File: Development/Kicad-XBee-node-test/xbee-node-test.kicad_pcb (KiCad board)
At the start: 2 copper layers, 90 x 50 mm, 48 parts, among them IC1 ATMEGA48-P, P1 Program, P2 Power 3.7V-12V, P3 Analogue, P4 Count, Q1 2N7002, Q2 BSS84, SW2 Commissioning, U1 TPS77033

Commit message: Minor tweaks on the PCBs ready to manufacture
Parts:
- added GND: GND, photodiode:SIL-1, F.Cu at (85.3, 96.7)
- added VRef: VRef, photodiode:SIL-1, F.Cu at (88.5, 68.4)
- moved G*** 1.31 mm to (71.7, 53.8)
- moved D1 0.77 mm to (82.5, 76.6)
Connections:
- D2 pad 1: GND -> Net-(D2-Pad1)
- D4 pad 1: GND -> Net-(D4-Pad1)
- D6 pad 1: GND -> Net-(D6-Pad1)
- D7 pad 1: GND -> Net-(D7-Pad1)
- R3 pad 1: Net-(D2-Pad2) -> Net-(R3-Pad1)
- R4 pad 1: Net-(D4-Pad2) -> Net-(R4-Pad1)
- R5 pad 1: Net-(D6-Pad2) -> Net-(R5-Pad1)
- R6 pad 1: Net-(D7-Pad2) -> Net-(R6-Pad1)
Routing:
- net Net-(D3-Pad1): track 3.08 -> 6.96 mm
- net Net-(R6-Pad1): track 0.00 -> 3.70 mm
- net Net-(R5-Pad1): track 0.00 -> 3.70 mm
- net Net-(R4-Pad1): track 0.00 -> 3.70 mm
- net Net-(R3-Pad1): track 0.00 -> 3.70 mm
- net Net-(D7-Pad2): track 4.78 -> 1.08 mm
- net Net-(D6-Pad2): track 4.78 -> 1.08 mm
- net Net-(D4-Pad2): track 4.78 -> 1.08 mm
- net Net-(D2-Pad2): track 4.78 -> 1.08 mm
- net /VBAT: track 87.6 -> 89.5 mm
- net /ARef: track 49.8 -> 50.7 mm
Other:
- board text added: "ATMega48/88/168/328"
- board text added: "Analogue"
- board text added: "Associate"
- board text added: "Commissioning"
- board text added: "Count"
- board text added: "Debug"
- board text added: "K. Sarkies Version 1 02/02/2017"
- board text added: "Power"
- board text added: "Power 3.7V - 12V"
- board text added: "Program"
- board text added: "Reset"
- board text added: "Test"
- board text added: "VRef Adjust"
- board text added: "XBee Node Test Board"

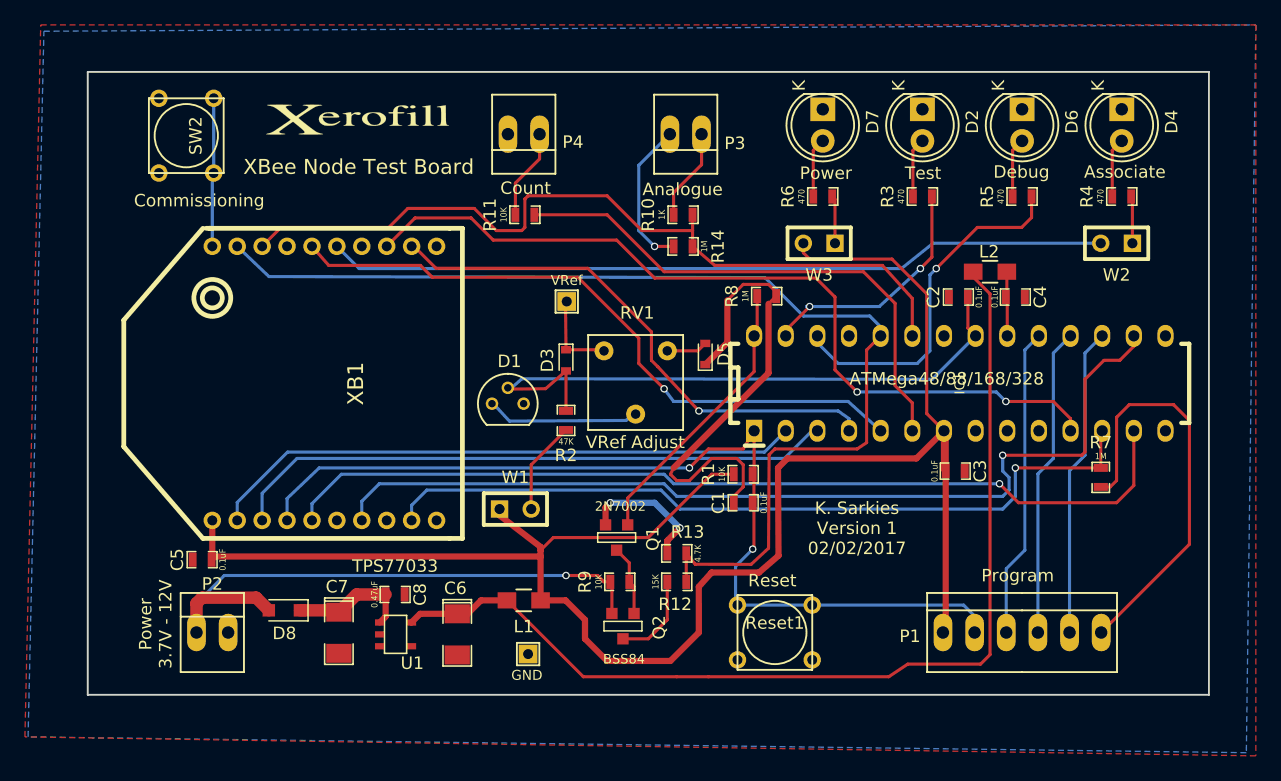
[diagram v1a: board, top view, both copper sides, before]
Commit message: Correct some stupid errors in Testboard and XBee-node-test PCBs.
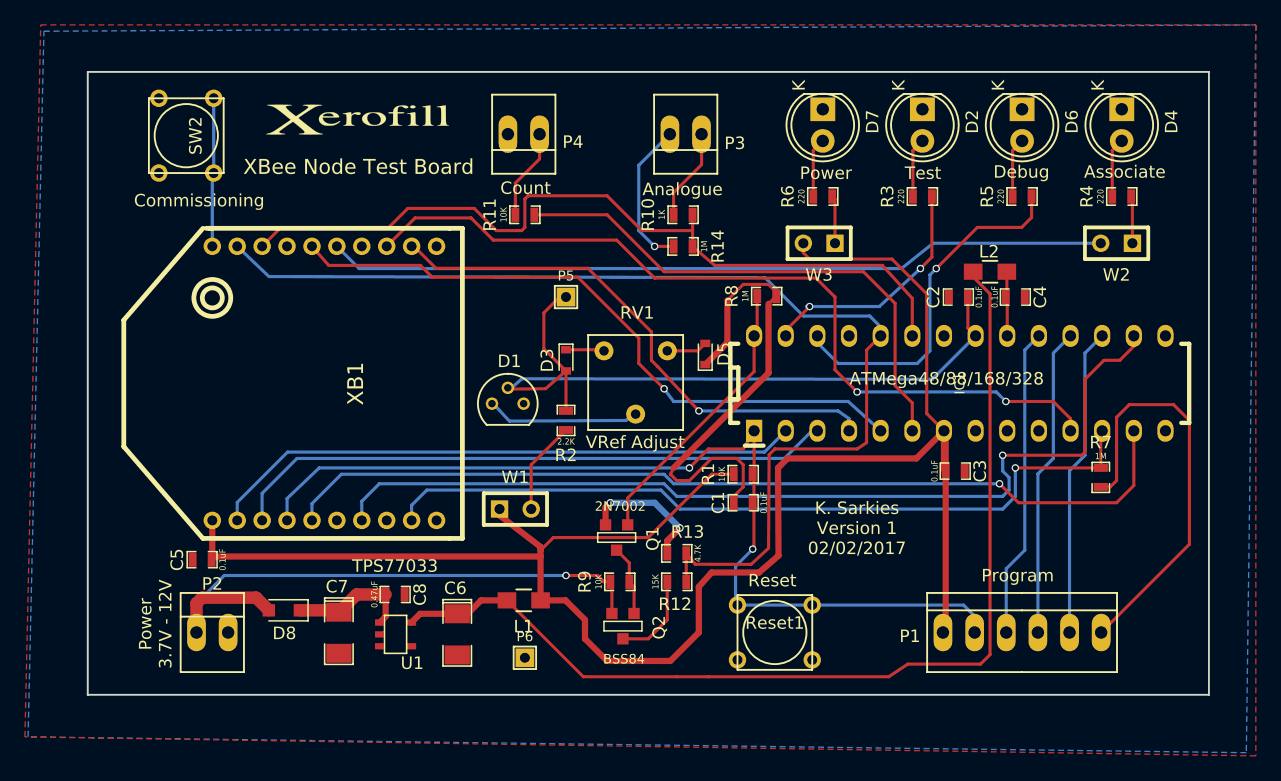
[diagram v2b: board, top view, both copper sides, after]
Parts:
- removed GND: GND, photodiode:SIL-1
- removed VRef: VRef, photodiode:SIL-1
- added P5: VRef, photodiode:SIL-1, F.Cu at (88.4, 68.1)
- added P6: GND, photodiode:SIL-1, F.Cu at (85.1, 97.0)
- D1: value LM336 -> LM336-2.5V
- D3, D5: value D -> 1N4148
- R2: value 47K -> 2.2K
- R3, R4, R5, R6: value 470 -> 220
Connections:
- D2 pad 1: Net-(D2-Pad1) -> GND
- D4 pad 1: Net-(D4-Pad1) -> GND
- D6 pad 1: Net-(D6-Pad1) -> GND
- D7 pad 1: Net-(D7-Pad1) -> GND
- R3 pad 1: Net-(R3-Pad1) -> Net-(D2-Pad2)
- R4 pad 1: Net-(R4-Pad1) -> Net-(D4-Pad2)
- R5 pad 1: Net-(R5-Pad1) -> Net-(D6-Pad2)
- R6 pad 1: Net-(R6-Pad1) -> Net-(D7-Pad2)
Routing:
- net /ARef: track 50.7 -> 58.4 mm
- net Net-(D3-Pad1): track 6.96 -> 3.08 mm
- net Net-(R6-Pad1): track 3.70 -> 0.00 mm
- net Net-(R5-Pad1): track 3.70 -> 0.00 mm
- net Net-(R4-Pad1): track 3.70 -> 0.00 mm
- net Net-(R3-Pad1): track 3.70 -> 0.00 mm
- net Net-(D7-Pad2): track 1.08 -> 4.78 mm
- net Net-(D6-Pad2): track 1.08 -> 4.78 mm
- net Net-(D4-Pad2): track 1.08 -> 4.78 mm
- net Net-(D2-Pad2): track 1.08 -> 4.78 mm
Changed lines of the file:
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@@
-(kicad_pcb (version 4) (host pcbnew 4.0.5-e0-6337~49~ubuntu16.04.1)
+(kicad_pcb (version 4) (host pcbnew 4.0.5-e0-6337~49~ubuntu14.04.1)
   (general
-    (links 95)
+    (links 103)
     (no_connects 0)
     (area 44.958 46.228 143.764001 104.902001)
     (thickness 1.6)
     (drawings 18)
-    (tracks 349)
+    (tracks 352)
     (zones 0)
     (modules 50)
-    (nets 61)
+    (nets 53)
   )
   (page A4)
   (layers
-    (0 F.Cu signal hide)
-    (31 B.Cu signal hide)
+    (0 F.Cu signal)
+    (31 B.Cu signal)
     (32 B.Adhes user hide)
     (33 F.Adhes user hide)
@@
   (net 51 "Net-(R4-Pad2)")
   (net 52 "Net-(R6-Pad2)")
-  (net 53 "Net-(D2-Pad1)")
-  (net 54 "Net-(D4-Pad1)")
-  (net 55 "Net-(D6-Pad1)")
-  (net 56 "Net-(D7-Pad1)")
-  (net 57 "Net-(R3-Pad1)")
-  (net 58 "Net-(R4-Pad1)")
-  (net 59 "Net-(R5-Pad1)")
-  (net 60 "Net-(R6-Pad1)")
   (net_class Default "This is the default net class."
     (clearance 0.2)
@@
     (add_net "Net-(C7-Pad1)")
     (add_net "Net-(D1-Pad1)")
-    (add_net "Net-(D2-Pad1)")
     (add_net "Net-(D2-Pad2)")
     (add_net "Net-(D3-Pad1)")
-    (add_net "Net-(D4-Pad1)")
     (add_net "Net-(D4-Pad2)")
     (add_net "Net-(D5-Pad2)")
-    (add_net "Net-(D6-Pad1)")
     (add_net "Net-(D6-Pad2)")
-    (add_net "Net-(D7-Pad1)")
     (add_net "Net-(D7-Pad2)")
     (add_net "Net-(IC1-Pad10)")
@@
     (add_net "Net-(Q2-PadD)")
     (add_net "Net-(R2-Pad1)")
-    (add_net "Net-(R3-Pad1)")
-    (add_net "Net-(R4-Pad1)")
     (add_net "Net-(R4-Pad2)")
-    (add_net "Net-(R5-Pad1)")
-    (add_net "Net-(R6-Pad1)")
     (add_net "Net-(R6-Pad2)")
     (add_net "Net-(U1-Pad4)")
@@
       (effects (font (size 1 1) (thickness 0.15)))
     )
-    (fp_text value LM336 (at 1.2 2.8) (layer F.Fab)
+    (fp_text value LM336-2.5V (at 1.2 2.8) (layer F.Fab)
       (effects (font (size 1 1) (thickness 0.15)))
     )
@@
     )
     (pad 1 thru_hole rect (at 0 0) (size 2 1.9) (drill 1) (layers *.Cu *.Mask F.SilkS)
-      (net 53 "Net-(D2-Pad1)"))
+      (net 2 GND))
     (pad 2 thru_hole circle (at 2.54 0 270) (size 1.9 1.9) (drill 1) (layers *.Cu *.Mask F.SilkS)
       (net 8 "Net-(D2-Pad2)"))
@@
       (effects (font (size 1 1) (thickness 0.15)))
     )
-    (fp_text value D (at -2.032 0 270) (layer F.Fab)
+    (fp_text value 1N4148 (at -2.032 0 270) (layer F.Fab)
       (effects (font (size 1 1) (thickness 0.15)))
     )
@@
     )
     (pad 1 thru_hole rect (at 0 0) (size 2 1.9) (drill 1) (layers *.Cu *.Mask F.SilkS)
-      (net 54 "Net-(D4-Pad1)"))
+      (net 2 GND))
     (pad 2 thru_hole circle (at 2.54 0 270) (size 1.9 1.9) (drill 1) (layers *.Cu *.Mask F.SilkS)
       (net 10 "Net-(D4-Pad2)"))
@@
       (effects (font (size 1 1) (thickness 0.15)))
     )
-    (fp_text value D (at 1.778 0 90) (layer F.Fab)
+    (fp_text value 1N4148 (at 1.778 0 90) (layer F.Fab)
       (effects (font (size 1 1) (thickness 0.15)))
     )
@@
     )
     (pad 1 thru_hole rect (at 0 0) (size 2 1.9) (drill 1) (layers *.Cu *.Mask F.SilkS)
-      (net 55 "Net-(D6-Pad1)"))
+      (net 2 GND))
     (pad 2 thru_hole circle (at 2.54 0 270) (size 1.9 1.9) (drill 1) (layers *.Cu *.Mask F.SilkS)
       (net 12 "Net-(D6-Pad2)"))
@@
     )
     (pad 1 thru_hole rect (at 0 0) (size 2 1.9) (drill 1) (layers *.Cu *.Mask F.SilkS)
-      (net 56 "Net-(D7-Pad1)"))
+      (net 2 GND))
     (pad 2 thru_hole circle (at 2.54 0 270) (size 1.9 1.9) (drill 1) (layers *.Cu *.Mask F.SilkS)
       (net 13 "Net-(D7-Pad2)"))
@@
       (effects (font (size 1 1) (thickness 0.15)))
     )
-    (fp_text value 47K (at -1.69926 0 180) (layer F.SilkS)
+    (fp_text value 2.2K (at -1.69926 0 180) (layer F.SilkS)
       (effects (font (size 0.508 0.4572) (thickness 0.1143)))
     )
@@
       (effects (font (size 1 1) (thickness 0.15)))
     )
-    (fp_text value 470 (at -1.69926 0 90) (layer F.SilkS)
+    (fp_text value 220 (at -1.69926 0 90) (layer F.SilkS)
       (effects (font (size 0.508 0.4572) (thickness 0.1143)))
     )
@@
     (fp_line (start 1.2065 0.6985) (end 0.50038 0.6985) (layer F.SilkS) (width 0.127))
     (pad 1 smd rect (at -0.762 0) (size 0.635 1.143) (layers F.Cu F.Paste F.Mask)
-      (net 57 "Net-(R3-Pad1)"))
+      (net 8 "Net-(D2-Pad2)"))
     (pad 2 smd rect (at 0.762 0) (size 0.635 1.143) (layers F.Cu F.Paste F.Mask)
       (net 32 /TEST))
@@
       (effects (font (size 1 1) (thickness 0.15)))
     )
-    (fp_text value 470 (at -1.69926 0 90) (layer F.SilkS)
+    (fp_text value 220 (at -1.69926 0 90) (layer F.SilkS)
       (effects (font (size 0.508 0.4572) (thickness 0.1143)))
     )
@@
     (fp_line (start 1.2065 0.6985) (end 0.50038 0.6985) (layer F.SilkS) (width 0.127))
     (pad 1 smd rect (at -0.762 0) (size 0.635 1.143) (layers F.Cu F.Paste F.Mask)
-      (net 58 "Net-(R4-Pad1)"))
+      (net 10 "Net-(D4-Pad2)"))
     (pad 2 smd rect (at 0.762 0) (size 0.635 1.143) (layers F.Cu F.Paste F.Mask)
       (net 51 "Net-(R4-Pad2)"))
@@
       (effects (font (size 1 1) (thickness 0.15)))
     )
-    (fp_text value 470 (at -1.69926 0 90) (layer F.SilkS)
+    (fp_text value 220 (at -1.69926 0 90) (layer F.SilkS)
       (effects (font (size 0.508 0.4572) (thickness 0.1143)))
     )
@@
     (fp_line (start 1.2065 0.6985) (end 0.50038 0.6985) (layer F.SilkS) (width 0.127))
     (pad 1 smd rect (at -0.762 0) (size 0.635 1.143) (layers F.Cu F.Paste F.Mask)
-      (net 59 "Net-(R5-Pad1)"))
+      (net 12 "Net-(D6-Pad2)"))
     (pad 2 smd rect (at 0.762 0) (size 0.635 1.143) (layers F.Cu F.Paste F.Mask)
       (net 34 /DEBUG))
@@
       (effects (font (size 1 1) (thickness 0.15)))
     )
-    (fp_text value 470 (at -1.69926 0 90) (layer F.SilkS)
+    (fp_text value 220 (at -1.69926 0 90) (layer F.SilkS)
       (effects (font (size 0.508 0.4572) (thickness 0.1143)))
     )
@@
     (fp_line (start 1.2065 0.6985) (end 0.50038 0.6985) (layer F.SilkS) (width 0.127))
     (pad 1 smd rect (at -0.762 0) (size 0.635 1.143) (layers F.Cu F.Paste F.Mask)
-      (net 60 "Net-(R6-Pad1)"))
+      (net 13 "Net-(D7-Pad2)"))
     (pad 2 smd rect (at 0.762 0) (size 0.635 1.143) (layers F.Cu F.Paste F.Mask)
       (net 52 "Net-(R6-Pad2)"))
@@
   )
   (module photodiode:SIL-1 (layer F.Cu)
-    (at 88.45 68.43)
+    (at 88.392 68.072)
     (descr "Connecteurs 1 pin")
     (tags "CONN DEV")
-    (fp_text reference VRef (at 0 -1.7) (layer F.SilkS)
+    (fp_text reference P5 (at 0 -1.7) (layer F.SilkS)
       (effects (font (size 0.8 0.8) (thickness 0.15)))
     )
@@
     (fp_line (start -0.9 0.9) (end -0.9 -0.9) (layer F.SilkS) (width 0.15))
     (pad 1 thru_hole rect (at 0 0) (size 1.5 1.5) (drill 0.8) (layers *.Cu *.Mask F.SilkS)
-      (net 9 "Net-(D3-Pad1)"))
+      (net 3 /ARef))
   )
   (module photodiode:SIL-1 (layer F.Cu)
-    (at 85.35 96.73)
+    (at 85.09 97.028)
     (descr "Connecteurs 1 pin")
     (tags "CONN DEV")
-    (fp_text reference GND (at -0.1 1.7) (layer F.SilkS)
+    (fp_text reference P6 (at 0 -1.7) (layer F.SilkS)
       (effects (font (size 0.8 0.8) (thickness 0.15)))
     )
@@
   (segment (start 104.648 74.168) (end 104.648 68.614) (width 0.5) (layer F.Cu) (net 2))
   (segment (start 104.648 68.614) (end 105.262 68) (width 0.25) (layer F.Cu) (net 2))
+  (segment (start 88.392 68.072) (end 87.884 68.072) (width 0.25) (layer F.Cu) (net 3))
+  (segment (start 87.884 68.072) (end 86.614 69.342) (width 0.25) (layer F.Cu) (net 3))
+  (segment (start 86.614 69.342) (end 86.614 72.224) (width 0.25) (layer F.Cu) (net 3))
+  (segment (start 86.614 72.224) (end 88.392 74.002) (width 0.25) (layer F.Cu) (net 3))
   (segment (start 120.65 68.072) (end 120.65 70.57) (width 0.25) (layer F.Cu) (net 3))
   (segment (start 120.65 70.57) (end 121.27 71.19) (width 0.25) (layer F.Cu) (net 3))
@@
   (segment (start 71.581 91.948) (end 70.16 93.369) (width 1) (layer F.Cu) (net 7))
   (segment (start 116.238 56.302) (end 117 55.54) (width 0.25) (layer F.Cu) (net 8))
-  (segment (start 88.35 68.43) (end 88.392 72.302) (width 0.25) (layer F.Cu) (net 9))
+  (segment (start 116.238 60) (end 116.238 56.302) (width 0.25) (layer F.Cu) (net 8))
   (segment (start 88.392 72.302) (end 91.352 72.302) (width 0.25) (layer F.Cu) (net 9))
   (segment (start 91.352 72.302) (end 91.44 72.39) (width 0.25) (layer F.Cu) (net 9))
   (segment (start 132.238 56.302) (end 133 55.54) (width 0.25) (layer F.Cu) (net 10))
+  (segment (start 132.238 60) (end 132.238 56.302) (width 0.25) (layer F.Cu) (net 10))
   (segment (start 96.52 72.39) (end 98.972 72.39) (width 0.25) (layer F.Cu) (net 11))
   (segment (start 98.972 72.39) (end 99.568 71.794) (width 0.25) (layer F.Cu) (net 11))
   (segment (start 124.238 56.302) (end 125 55.54) (width 0.25) (layer F.Cu) (net 12))
+  (segment (start 124.238 60) (end 124.238 56.302) (width 0.25) (layer F.Cu) (net 12))
   (segment (start 108.238 56.302) (end 109 55.54) (width 0.25) (layer F.Cu) (net 13))
+  (segment (start 108.238 60) (end 108.238 56.302) (width 0.25) (layer F.Cu) (net 13))
   (segment (start 58.73 95) (end 58.73 92.654) (width 1) (layer F.Cu) (net 14))
   (segment (start 63.52 92.202) (end 64.536 93.218) (width 1) (layer F.Cu) (net 14))
@@
   (segment (start 109.982 63.754) (end 109.982 60.22) (width 0.25) (layer F.Cu) (net 52))
   (segment (start 109.982 60.22) (end 109.762 60) (width 0.25) (layer F.Cu) (net 52))
-  (segment (start 116.238 60) (end 116.238 56.302) (width 0.25) (layer F.Cu) (net 57))
-  (segment (start 132.238 60) (end 132.238 56.302) (width 0.25) (layer F.Cu) (net 58))
-  (segment (start 124.238 60) (end 124.238 56.302) (width 0.25) (layer F.Cu) (net 59))
-  (segment (start 108.238 60) (end 108.238 56.302) (width 0.25) (layer F.Cu) (net 60))
   (zone (net 2) (net_name GND) (layer F.Cu) (hatch edge 0.508)
     (connect_pads (clearance 0.508))
